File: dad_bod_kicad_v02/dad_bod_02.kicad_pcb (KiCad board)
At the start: 2 copper layers, 98.5 x 69.9 mm, 135 parts, among them J1 Conn_01x01, J10 Conn_01x03_Male, J11 BNC5-J-P-GN-RA-BH2D, J12 USB4085-GF-A_REVA4, J13 Conn_01x03_Male, J2 Conn_01x01, J3 Conn_01x01, J4 Conn_01x01, J5 Conn_01x03_Male, J6 Conn_02x15_Odd_Even, J7 BNC5-J-P-GN-RA-BH2D, J8 Conn_01x03_Male, J9 Conn_02x15_Odd_Even, K1 EC2-5NU, K2 EC2-5NU, Q1 2N3904, Q2 2N3904, Q3 AO3401A, T1 GT07-110-013, U1 SL1002A600SP, U2 LTC6269, U3 LTC6268, U4 LM7301

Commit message: Added sketches & iterations
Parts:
- moved J9 61.5 mm to (198.1, 74.2)
- moved J6 60.6 mm to (201.8, 74.2)
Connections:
- net PLCin+ renamed DIVin2-
- net PLCin- renamed DIVin2+
- net PLCout- renamed BNCin-
- J6 pad 1: scope1- -> scope1+
- J6 pad 10: waveform1 -> waveform2
- J6 pad 13: trigger2 -> trigger1
- J6 pad 14: trigger1 -> trigger2
- J6 pad 15: 8 -> 0
- J6 pad 16: 0 -> 8
- J6 pad 17: 9 -> 1
- J6 pad 18: 1 -> 9
- J6 pad 19: 10 -> 2
- J6 pad 2: scope1+ -> scope1-
- J6 pad 20: 2 -> 10
- J6 pad 21: 11 -> 3
- J6 pad 22: 3 -> 11
- J6 pad 23: 12 -> 4
- J6 pad 24: 4 -> 12
- J6 pad 25: 13 -> 5
- J6 pad 26: 5 -> 13
- J6 pad 27: 14 -> CV6
- J6 pad 28: CV6 -> 14
- J6 pad 29: 15 -> CV7
- J6 pad 3: scope2- -> scope2+
- J6 pad 30: CV7 -> 15
- J6 pad 4: scope2+ -> scope2-
- J6 pad 7: dad_V- -> relaypwr
- J6 pad 8: relaypwr -> dad_V-
- J6 pad 9: waveform2 -> waveform1
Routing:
- net GND: track 295.4 -> 0.00 mm, vias 3 -> 0
- net BNCin-: track 164.2 -> 0.00 mm, vias 1 -> 0
- net VCC: track 157.5 -> 0.00 mm, vias 6 -> 0
- net greg: track 152.8 -> 0.00 mm, vias 9 -> 0
- net relaypwr: track 133.5 -> 0.00 mm
- net DIVin2-: track 117.9 -> 0.00 mm, vias 2 -> 0
- net PLCout+: track 116.9 -> 0.00 mm, vias 3 -> 0
- net GNDREF: track 113.8 -> 0.00 mm, vias 4 -> 0
- net DIVout1+: track 109.3 -> 0.00 mm, vias 4 -> 0
- net DIVout1-: track 95.5 -> 0.00 mm, vias 4 -> 0
- net DIVin2+: track 80.9 -> 0.00 mm
- net CV6: track 80.4 -> 0.00 mm
- net DIVout2+: track 78.6 -> 0.00 mm
- net DIVout2-: track 78.0 -> 0.00 mm
- net scope2+: track 55.4 -> 0.00 mm
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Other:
- board outline removed

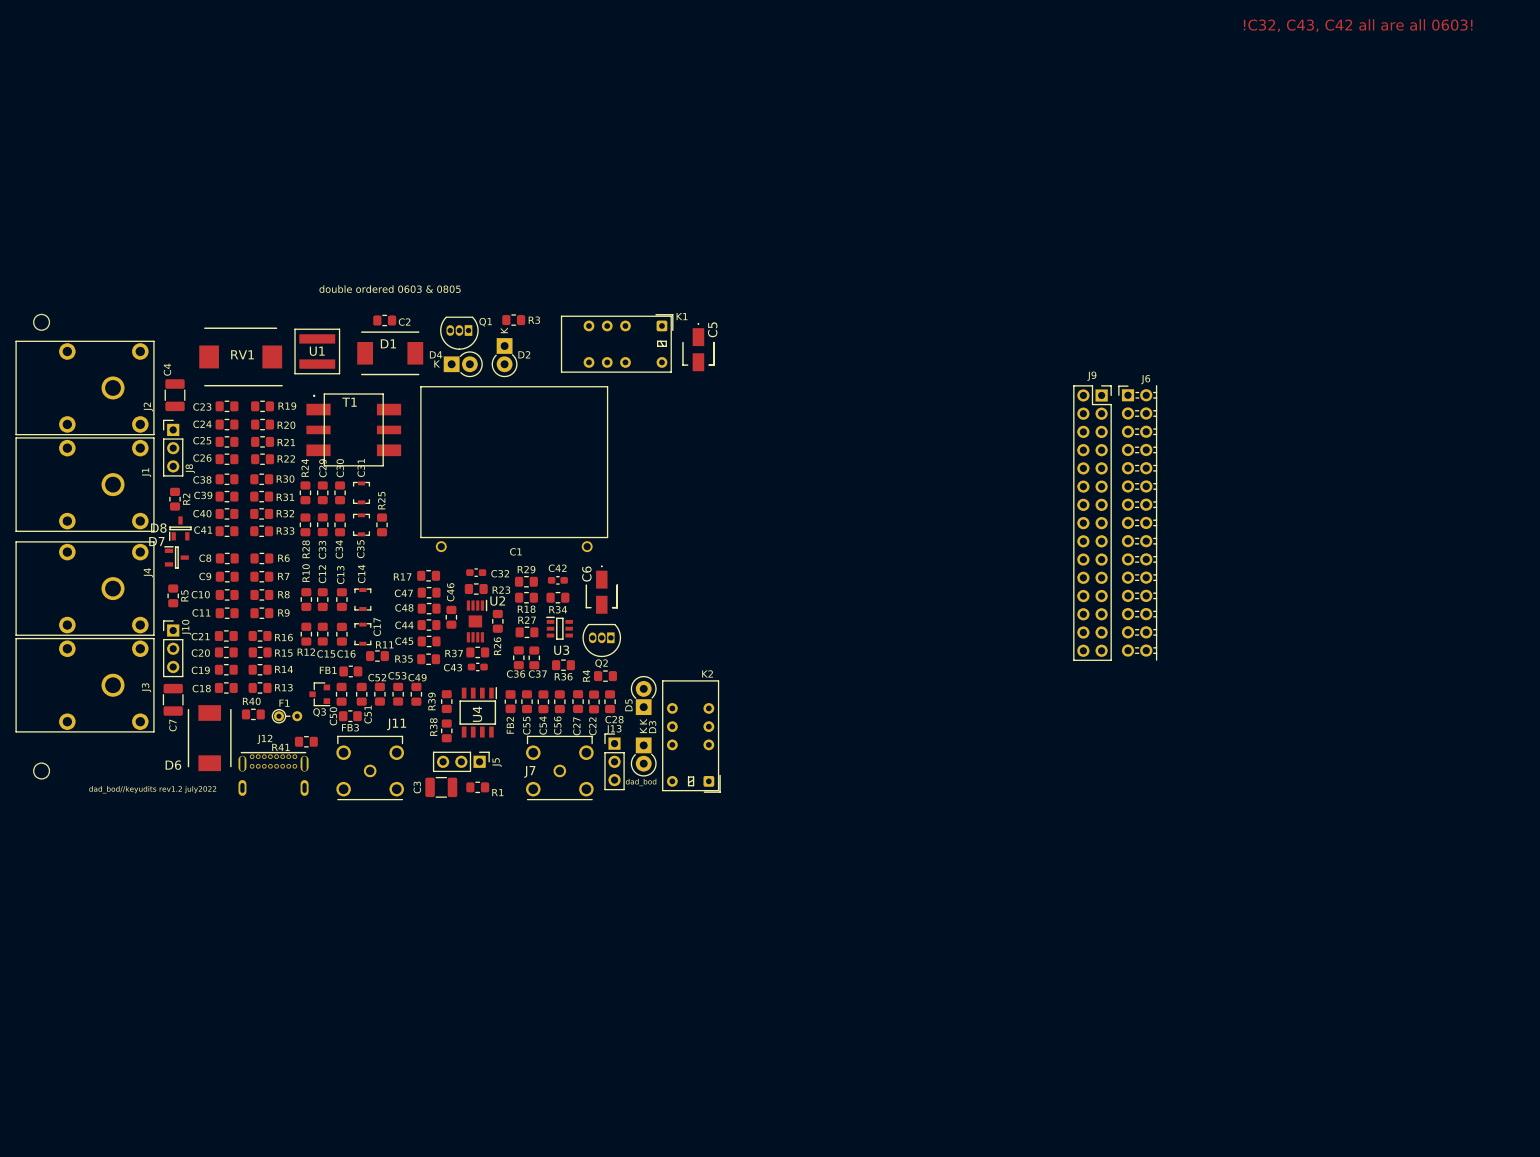
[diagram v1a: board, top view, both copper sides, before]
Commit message: Finished dad_bod_v02 layout, awaiting routing
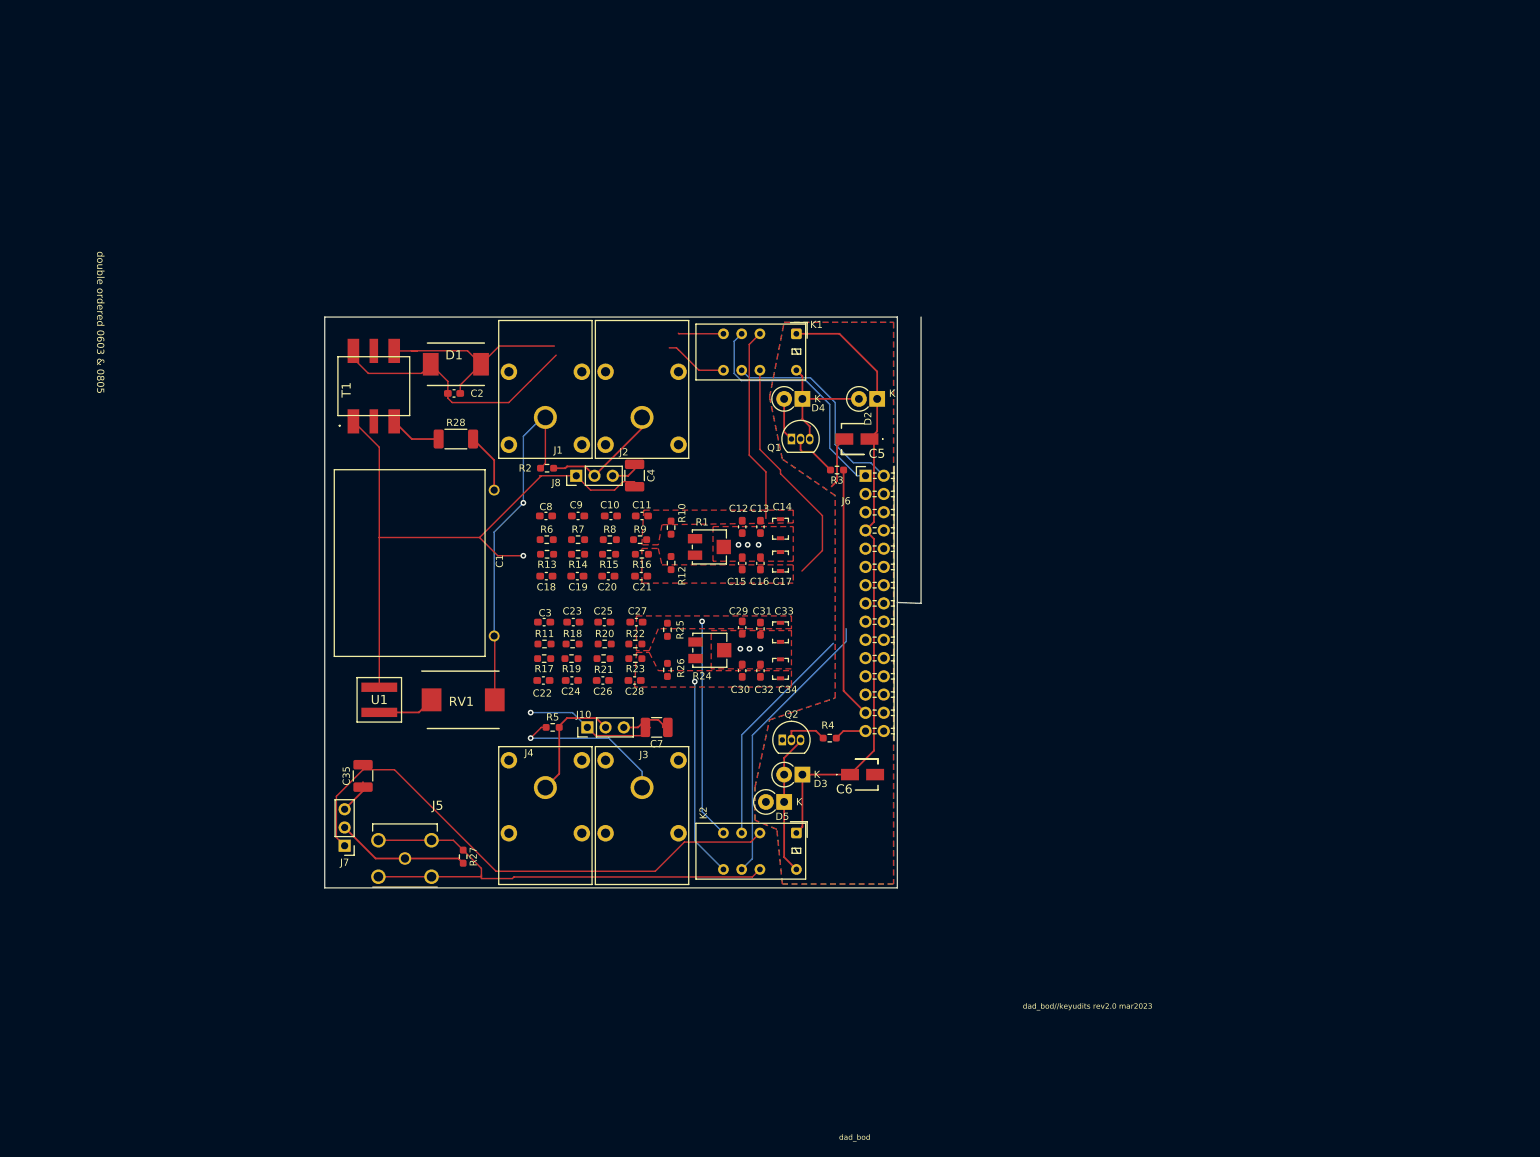
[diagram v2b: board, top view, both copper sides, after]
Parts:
- removed C36, C37, C44, C45, C46, C47, C48, C49, C50, C51, C52, C53, C54, C55, C56: ~, Capacitor_SMD:C_0805_2012Metric_Pad1.15x1.40mm_HandSolder
- removed C38, C39, C40, C41: 4pf, Capacitor_SMD:C_0805_2012Metric_Pad1.15x1.40mm_HandSolder
- removed C42, C43: ~, Capacitor_SMD:C_0603_1608Metric_Pad1.05x0.95mm_HandSolder
- removed D6: SMCJ5.0A, kyuditsky_kicad_fp:littlefuseTVS
- removed D7, D8: BAV199-TP, kyuditsky_kicad:bav199_tp_SOT95P237X125-3N
- removed F1: 2.5a Fuse, Resistor_THT:R_Axial_DIN0204_L3.6mm_D1.6mm_P2.54mm_Vertical
- removed FB1, FB2, FB3: Ferrite_Bead, Resistor_SMD:R_0805_2012Metric_Pad1.20x1.40mm_HandSolder
- removed J11: BNC5-J-P-GN-RA-BH2D, BNC5-J-P-GN-RA-BH2D_kicad:BNC5JPGNRABH2D
- removed J12: USB4085-GF-A_REVA4, kyuditsky_kicad:GCT_USB4085-GF-A_REVA4
- removed J13: Conn_01x03_Male, Connector_PinHeader_2.54mm:PinHeader_1x03_P2.54mm_Vertical
- removed J9: Conn_02x15_Odd_Even, Connector_PinSocket_2.54mm:PinSocket_2x15_P2.54mm_Vertical
- removed Q3: AO3401A, Package_TO_SOT_SMD:SOT-23
- removed R29, R34, R35, R36, R37, R38, R39: ~, Resistor_SMD:R_0805_2012Metric_Pad1.15x1.40mm_HandSolder
- removed R30, R31, R32, R33: 1M, Resistor_SMD:R_0805_2012Metric_Pad1.15x1.40mm_HandSolder
- removed R40, R41: 5.1k, Resistor_SMD:R_0805_2012Metric_Pad1.15x1.40mm_HandSolder
- removed REF** (x2): MountingHole_2.2mm_M2, MountingHole:MountingHole_2.2mm_M2
- removed U2: LTC6269, kyuditsky_kicad_fp:SOP65P490X110-9N_LTC6269
- removed U3: LTC6268, kyuditsky_kicad_fp:SOT95P280X100-6N_LTC6268
- removed U4: LM7301, kyuditsky_kicad_fp:SOIC127P600X175-8NLM7301
- C10, C11, C12, C13, C15, C16, C18, C19, C2, C20, C21, C23, C24, C25, C26, C29, C30, C8, C9: footprint Capacitor_SMD:C_0805_2012Metric_Pad1.15x1.40mm_HandSolder -> Capacitor_SMD:C_0603_1608Metric_Pad1.08x0.95mm_HandSolder
- C22, C27, C28: value ~ -> 4pf; footprint Capacitor_SMD:C_0805_2012Metric_Pad1.15x1.40mm_HandSolder -> Capacitor_SMD:C_0603_1608Metric_Pad1.08x0.95mm_HandSolder
- C3: value 86nF -> 4pf; footprint Capacitor_SMD:C_1210_3225Metric_Pad1.33x2.70mm_HandSolder -> Capacitor_SMD:C_0603_1608Metric_Pad1.08x0.95mm_HandSolder
- C31: value CTRIM -> 350pF; footprint Capacitor_SMD:C_Trimmer_Voltronics_JQ -> Capacitor_SMD:C_0603_1608Metric_Pad1.08x0.95mm_HandSolder
- C32: value ~ -> 350pF; footprint Capacitor_SMD:C_0603_1608Metric_Pad1.05x0.95mm_HandSolder -> Capacitor_SMD:C_0603_1608Metric_Pad1.08x0.95mm_HandSolder
- C33, C34: value 350pF -> CTRIM; footprint Capacitor_SMD:C_0805_2012Metric_Pad1.15x1.40mm_HandSolder -> Capacitor_SMD:C_Trimmer_Voltronics_JQ
- C35: value CTRIM -> 86nF; footprint Capacitor_SMD:C_Trimmer_Voltronics_JQ -> Capacitor_SMD:C_1210_3225Metric_Pad1.33x2.70mm_HandSolder
- J5: value Conn_01x03_Male -> BNC5-J-P-GN-RA-BH2D; footprint Connector_PinHeader_2.54mm:PinHeader_1x03_P2.54mm_Vertical -> kyuditsky_kicad:BNC5JPGNRABH2D
- J7: value BNC5-J-P-GN-RA-BH2D -> Conn_01x03_Male; footprint BNC5-J-P-GN-RA-BH2D_kicad:BNC5JPGNRABH2D -> Connector_PinHeader_2.54mm:PinHeader_1x03_P2.54mm_Vertical
- R1: value 30M -> rv2; footprint Resistor_SMD:R_0805_2012Metric_Pad1.15x1.40mm_HandSolder -> Potentiometer_SMD:Potentiometer_Bourns_3314J_Vertical
- R10, R12, R13, R14, R15, R16, R19, R2, R20, R21, R22, R3, R4, R5, R6, R7, R8, R9: footprint Resistor_SMD:R_0805_2012Metric_Pad1.15x1.40mm_HandSolder -> Resistor_SMD:R_0603_1608Metric_Pad0.98x0.95mm_HandSolder
- R11: value DNP -> 1M; footprint Resistor_SMD:R_0805_2012Metric_Pad1.15x1.40mm_HandSolder -> Resistor_SMD:R_0603_1608Metric_Pad0.98x0.95mm_HandSolder
- R17, R18, R23: value ~ -> 1M; footprint Resistor_SMD:R_0805_2012Metric_Pad1.15x1.40mm_HandSolder -> Resistor_SMD:R_0603_1608Metric_Pad0.98x0.95mm_HandSolder
- R24: value 50k -> rv1; footprint Resistor_SMD:R_0805_2012Metric_Pad1.15x1.40mm_HandSolder -> Potentiometer_SMD:Potentiometer_Bourns_3314J_Vertical
- R25: value DNP -> 50k; footprint Resistor_SMD:R_0805_2012Metric_Pad1.15x1.40mm_HandSolder -> Resistor_SMD:R_0603_1608Metric_Pad0.98x0.95mm_HandSolder
- R26: value ~ -> 50k; footprint Resistor_SMD:R_0805_2012Metric_Pad1.15x1.40mm_HandSolder -> Resistor_SMD:R_0603_1608Metric_Pad0.98x0.95mm_HandSolder
- R27: value ~ -> 30M; footprint Resistor_SMD:R_0805_2012Metric_Pad1.15x1.40mm_HandSolder -> Resistor_SMD:R_0603_1608Metric_Pad0.98x0.95mm_HandSolder
- R28: value 50k -> 2.2; footprint Resistor_SMD:R_0805_2012Metric_Pad1.15x1.40mm_HandSolder -> Resistor_SMD:R_2010_5025Metric_Pad1.40x2.65mm_HandSolder
- moved J3 75.0 mm to (134.1, 128.8), turned to -90 degrees
- moved J2 73.8 mm to (134.1, 77.3), turned to 90 degrees
- moved C7 67.4 mm to (136.2, 120.4), turned to 180 degrees
- moved J4 66.3 mm to (120.7, 128.8), turned to -90 degrees
- moved C33 65.5 mm to (153.4, 107.2), turned to -90 degrees
- moved C4 65.0 mm to (133.1, 85.3), turned to -90 degrees
- moved C34 64.5 mm to (153.4, 112.3), turned to -90 degrees
- moved C29 61.4 mm to (148.1, 106.5)
- moved C30 61.2 mm to (148.1, 112.5)
- moved J1 60.9 mm to (120.7, 77.3), turned to 90 degrees
- moved C26 60.7 mm to (128.7, 113.9)
- moved R24 60.4 mm to (143.6, 109.7)
- moved C24 59.8 mm to (124.4, 113.9)
- moved C11 59.3 mm to (134.1, 91.0), turned to 180 degrees
- moved C12 59.3 mm to (148.1, 92.5)
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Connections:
- C12 pad 1: Net-(C12-Pad1) -> GNDREF
- C13 pad 1: Net-(C12-Pad1) -> GNDREF
- C14 pad 2: Net-(C12-Pad1) -> GNDREF
- C15 pad 2: Net-(C12-Pad1) -> GNDREF
- C16 pad 2: Net-(C12-Pad1) -> GNDREF
- C17 pad 1: Net-(C12-Pad1) -> GNDREF
- C2 pad 1: BNCin- -> PLCout-
- C22 pad 1: GNDREF -> DIVin1-
- C22 pad 2: VCC -> Net-(C22-Pad2)
- C23 pad 2: DIVin1+ -> Net-(C23-Pad2)
- C24 pad 1: Net-(C24-Pad1) -> Net-(C22-Pad2)
- C24 pad 2: Net-(C23-Pad1) -> Net-(C24-Pad2)
- C25 pad 2: Net-(C24-Pad1) -> Net-(C23-Pad1)
- C26 pad 1: DIVout1+ -> Net-(C24-Pad2)
- C26 pad 2: Net-(C25-Pad1) -> Net-(C26-Pad2)
- C27 pad 1: VCC -> DIVout1+
- C27 pad 2: greg -> Net-(C25-Pad1)
- C28 pad 1: GNDREF -> Net-(C26-Pad2)
- C28 pad 2: VCC -> DIVout1-
- C29 pad 1: Net-(C29-Pad1) -> GNDREF
- C3 pad 1: Net-(C3-Pad1) -> Net-(C23-Pad2)
- C3 pad 2: BNCin+ -> DIVin1+
- C30 pad 1: Net-(C29-Pad1) -> DIVout1-
- C30 pad 2: DIVout1+ -> GNDREF
- C31 pad 1: DIVout1+ -> GNDREF
- C31 pad 2: Net-(C29-Pad1) -> DIVout1+
- C32 pad 1: Net-(C32-Pad1) -> DIVout1-
- C32 pad 2: Net-(C32-Pad2) -> GNDREF
- C33 pad 1: DIVout1- -> DIVout1+
- C33 pad 2: Net-(C29-Pad1) -> GNDREF
- C34 pad 1: DIVout1- -> GNDREF
- C34 pad 2: Net-(C29-Pad1) -> DIVout1-
- C35 pad 1: Net-(C29-Pad1) -> Net-(C35-Pad1)
- C35 pad 2: DIVout1- -> BNCin+
- D1 pad 2: BNCin- -> PLCout-
- J5 pad 1: BNCin+ -> bnc_imp+
- J5 pad 2: bnc_imp+ -> BNCin-
- J5 pad 3: Net-(C3-Pad1) -> BNCin-
- J7 pad 1: Net-(J13-Pad2) -> BNCin+
- J7 pad 2: BNCin- -> bnc_imp+
- J7 pad 3: BNCin- -> Net-(C35-Pad1)
- K1 pad 8: BNCin- -> PLCout-
- R1 pad 1: BNCin- -> Net-(R1-Pad1)
- R1 pad 2: bnc_imp+ -> GNDREF
- R10 pad 1: Net-(C12-Pad1) -> Net-(R1-Pad1)
- R11 pad 1: GNDREF -> DIVin1+
- R11 pad 2: Net-(C12-Pad1) -> Net-(R11-Pad2)
- R12 pad 2: Net-(C12-Pad1) -> Net-(R1-Pad3)
- R17 pad 2: DIVout1+ -> DIVin1-
- R18 pad 1: Net-(R18-Pad1) -> Net-(R11-Pad2)
- R18 pad 2: Net-(C32-Pad1) -> Net-(R18-Pad2)
- R19 pad 1: DIVin1+ -> Net-(R19-Pad1)
- R19 pad 2: Net-(R19-Pad2) -> Net-(R17-Pad1)
- R20 pad 1: Net-(R19-Pad2) -> Net-(R18-Pad2)
- R21 pad 1: Net-(R20-Pad2) -> Net-(R21-Pad1)
- R21 pad 2: Net-(R21-Pad2) -> Net-(R19-Pad1)
- R22 pad 1: Net-(R21-Pad2) -> Net-(R20-Pad2)
- R23 pad 1: Net-(C32-Pad1) -> DIVout1-
- R23 pad 2: Net-(C32-Pad2) -> Net-(R21-Pad1)
- R24 pad 1: Net-(C29-Pad1) -> Net-(R24-Pad1)
- R24 pad 2: DIVout1+ -> GNDREF
- R25 pad 1: GNDREF -> Net-(R24-Pad1)
- R25 pad 2: Net-(C29-Pad1) -> DIVout1+
- R26 pad 1: Net-(C43-Pad2) -> DIVout1-
- R26 pad 2: Net-(C32-Pad2) -> Net-(R24-Pad3)
- R27 pad 1: Net-(J11-Pad1) -> BNCin-
- R27 pad 2: Net-(C42-Pad1) -> bnc_imp+
- R28 pad 1: DIVout1- -> Net-(T1-Pad3)
- R28 pad 2: Net-(C29-Pad1) -> Net-(C1-Pad2)
- T1 pad 3: Net-(C1-Pad2) -> Net-(T1-Pad3)
- T1 pad 4: BNCin- -> PLCout-
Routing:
- net relaypwr: track 0.00 -> 87.7 mm
- net DIVin2-: track 0.00 -> 86.5 mm, vias 0 -> 1
- net BNCin+: track 0.00 -> 75.9 mm
- net BNCin-: track 0.00 -> 71.3 mm
- net DIVin2+: track 0.00 -> 49.9 mm, vias 0 -> 1
- net PLCout+: track 0.00 -> 43.3 mm
- net scope2-: track 0.00 -> 39.6 mm
- net PLCout-: track 0.00 -> 39.1 mm
- net CV6: track 0.00 -> 35.1 mm
- net scope1+: track 0.00 -> 33.7 mm
- net DIVout2-: track 0.00 -> 32.8 mm
- net scope2+: track 0.00 -> 31.7 mm
- net DIVout1+: track 0.00 -> 30.7 mm, vias 0 -> 1
- net scope1-: track 0.00 -> 29.3 mm
- net DIVout1-: track 0.00 -> 27.8 mm, vias 0 -> 1
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- added copper zone on F.Cu, net DIVout1+
- added copper zone on F.Cu, net DIVout1-
- added copper zone on F.Cu, net DIVout2+
- added copper zone on F.Cu, net DIVout2-
- added copper zone on B.Cu, net GND
- added copper zone on F.Cu, net GND
- added copper zone on F.Cu, net GNDREF
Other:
- board outline added: 83.1 x 79.5 mm
- board text added: "dad_bod//keyudits rev2.0 mar2023"
- board text added: "the whole header assembly doesnt really need to be on this board it can be taken care on the daughter board just a thought"
- board text removed: "!C32, C43, C42 all are all 0603!"
- board text removed: "dad_bod//keyudits rev1.2 july2022"

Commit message: Added beach_bod troubleshooting video
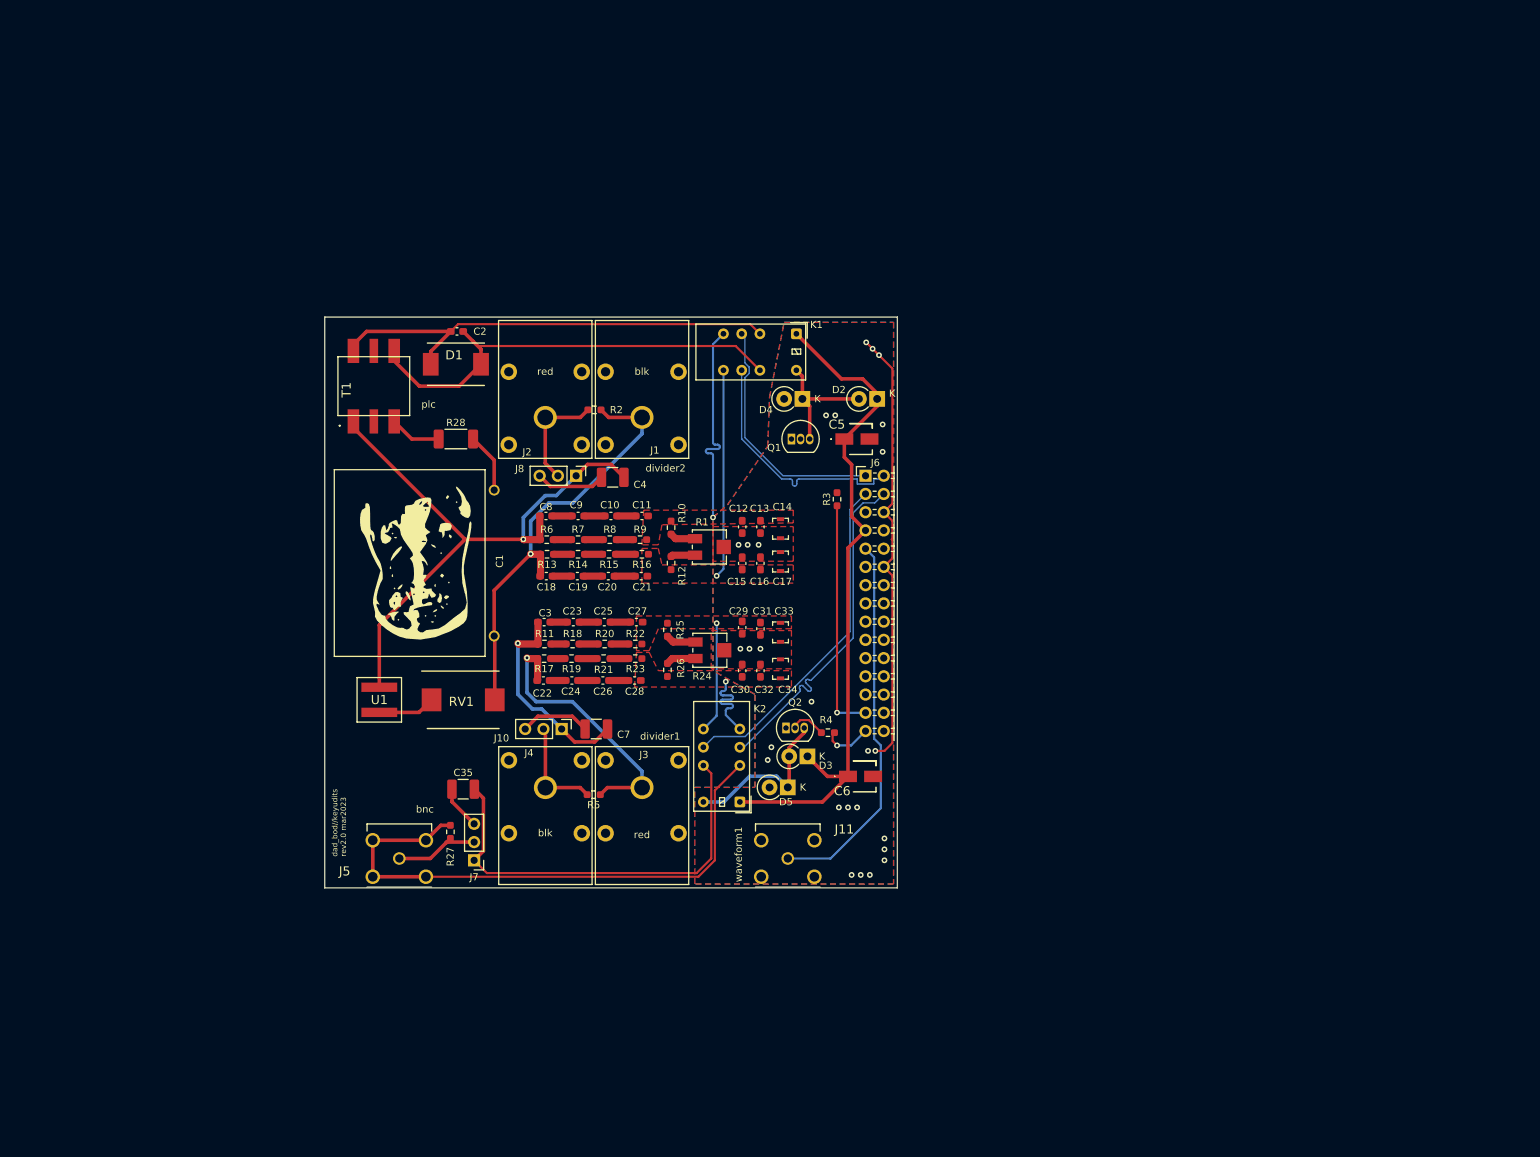
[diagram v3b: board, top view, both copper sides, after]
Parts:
- added G***: LOGO, kyuditsky_kicad:dad_body, F.Cu at (105.2, 97.9)
- added G***: LOGO, kyuditsky_kicad:dad_bod, B.Cu at (138.8, 104.1)
- added J11: BNC5-J-P-GN-RA-BH2D, kyuditsky_kicad:BNC5JPGNRABH2D, F.Cu at (154.4, 138.7)
- moved J7 18.1 mm to (110.7, 138.9)
- moved C35 14.1 mm to (109.2, 129.0), turned to 0 degrees
- moved J2 13.5 mm to (120.7, 77.3)
- moved J1 13.5 mm to (134.1, 77.3)
- moved R5 11.0 mm to (127.4, 129.8), turned to 180 degrees
- moved R2 10.5 mm to (127.5, 76.2), turned to 180 degrees
- moved K2 8.98 mm to (147.8, 130.8), turned to 180 degrees
- moved C2 8.65 mm to (108.4, 65.3)
- moved C7 8.40 mm to (127.8, 120.7), turned to 0 degrees
- moved R3 4.06 mm to (161.3, 88.6), turned to 90 degrees
- moved R27 3.88 mm to (107.4, 135.0)
- moved J10 3.58 mm to (122.9, 120.7), turned to -90 degrees
- moved C4 3.06 mm to (130.0, 85.6), turned to 0 degrees
- moved D3 2.64 mm to (157.2, 124.5)
- moved D5 2.09 mm to (154.4, 128.8)
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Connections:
- C1 pad 1: DIVin2+ -> DIVin2-
- C12 pad 1: GNDREF -> GND
- C13 pad 1: GNDREF -> GND
- C14 pad 2: GNDREF -> GND
- C15 pad 2: GNDREF -> GND
- C16 pad 2: GNDREF -> GND
- C17 pad 1: GNDREF -> GND
- C29 pad 1: GNDREF -> GND
- C30 pad 2: GNDREF -> GND
- C31 pad 1: GNDREF -> GND
- C32 pad 2: GNDREF -> GND
- C33 pad 2: GNDREF -> GND
- C34 pad 1: GNDREF -> GND
- C4 pad 2: DIVin2- -> DIVin2+
- J1 pad 1: DIVin2+ -> DIVin2-
- J8 pad 1: DIVin2- -> DIVin2+
- K1 pad 10: DIVout2- -> PLCout-
- K1 pad 3: DIVout2+ -> PLCout+
- K1 pad 5: PLCout+ -> DIVout2+
- K1 pad 8: PLCout- -> DIVout2-
- K2 pad 10: BNCin- -> BNCin+
- K2 pad 3: BNCin+ -> BNCin-
- K2 pad 4: scope2+ -> scope2-
- K2 pad 5: DIVout1+ -> DIVout1-
- K2 pad 8: DIVout1- -> DIVout1+
- K2 pad 9: scope2- -> scope2+
- Q1 pad 2: Net-(Q1-Pad2) -> unconnected-(Q1-Pad2)
- R1 pad 2: GNDREF -> GND
- R2 pad 1: DIVin2+ -> DIVin2-
- R24 pad 2: GNDREF -> GND
- RV1 pad 2: DIVin2+ -> DIVin2-
- T1 pad 1: DIVin2- -> DIVin2+
- U1 pad 2: DIVin2- -> DIVin2+
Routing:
- net waveform1: track 0.00 -> 52.4 mm
- net GND: track 13.3 -> 62.2 mm, vias 0 -> 27
- net DIVin2+: track 49.9 -> 82.2 mm
- net DIVin2-: track 86.5 -> 60.3 mm
- net PLCout-: track 39.1 -> 62.0 mm
- net PLCout+: track 43.3 -> 64.1 mm
- net BNCin+: track 75.9 -> 59.0 mm
- net DIVin1-: track 22.5 -> 38.5 mm
- net scope2+: track 31.7 -> 47.2 mm
- net DIVout1+: track 30.7 -> 15.5 mm
- net DIVout1-: track 27.8 -> 13.0 mm
- net Net-(C7-Pad1): track 0.00 -> 9.82 mm
- net BNCin-: track 71.3 -> 80.0 mm
- net scope2-: track 39.6 -> 47.3 mm
- net relaypwr: track 87.7 -> 94.7 mm
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- removed copper zone on F.Cu, net GNDREF
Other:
- board size 83.1 x 79.5 mm -> 79.8 x 79.5 mm
- rule pad_to_mask_clearance: 0.05 -> 0
- board text added: "03/20/23"
- board text added: "blk"
- board text added: "bnc"
- board text added: "dad_bod_v02"
- board text added: "divider1"
- board text added: "divider2"
- board text added: "plc"
- board text added: "red"
- board text added: "waveform1"
- board text removed: "dad_bod"
- board text removed: "double ordered 0603 & 0805"
